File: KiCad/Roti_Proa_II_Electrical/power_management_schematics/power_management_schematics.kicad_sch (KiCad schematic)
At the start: 0 parts

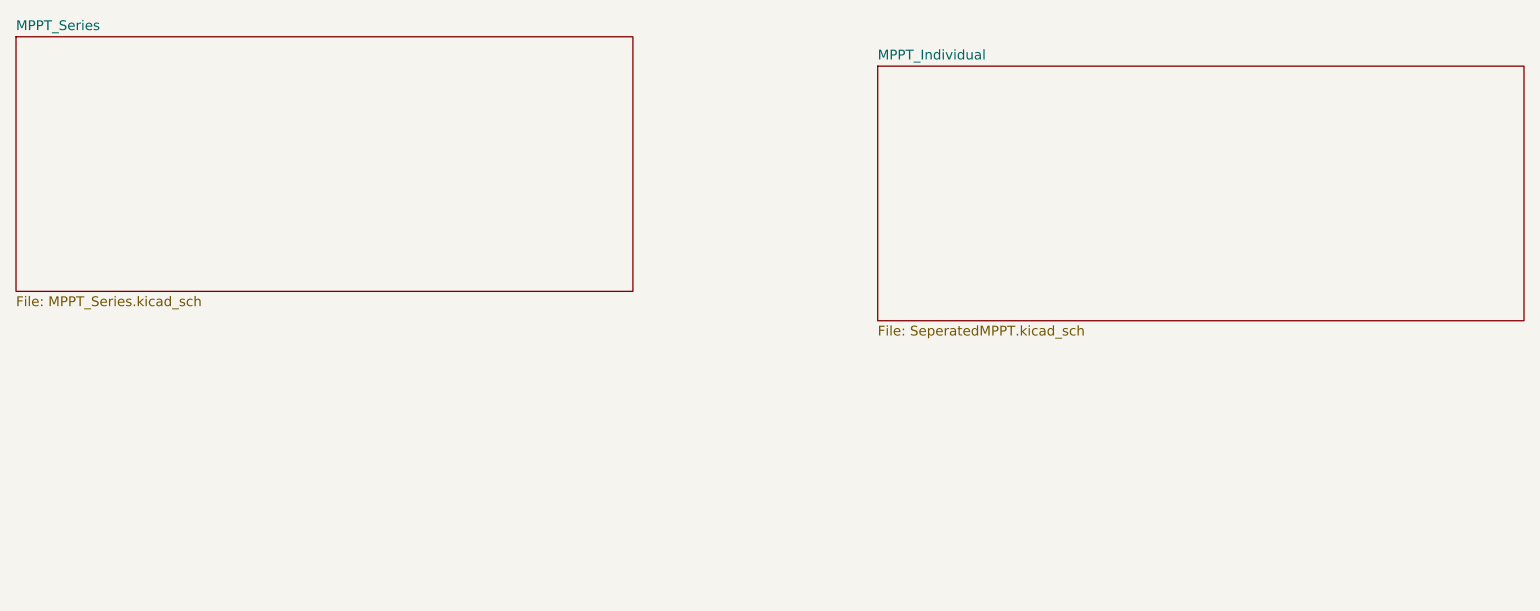
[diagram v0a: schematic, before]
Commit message: Complete MPPT+HE reading
Reading works for arduino and esp8266
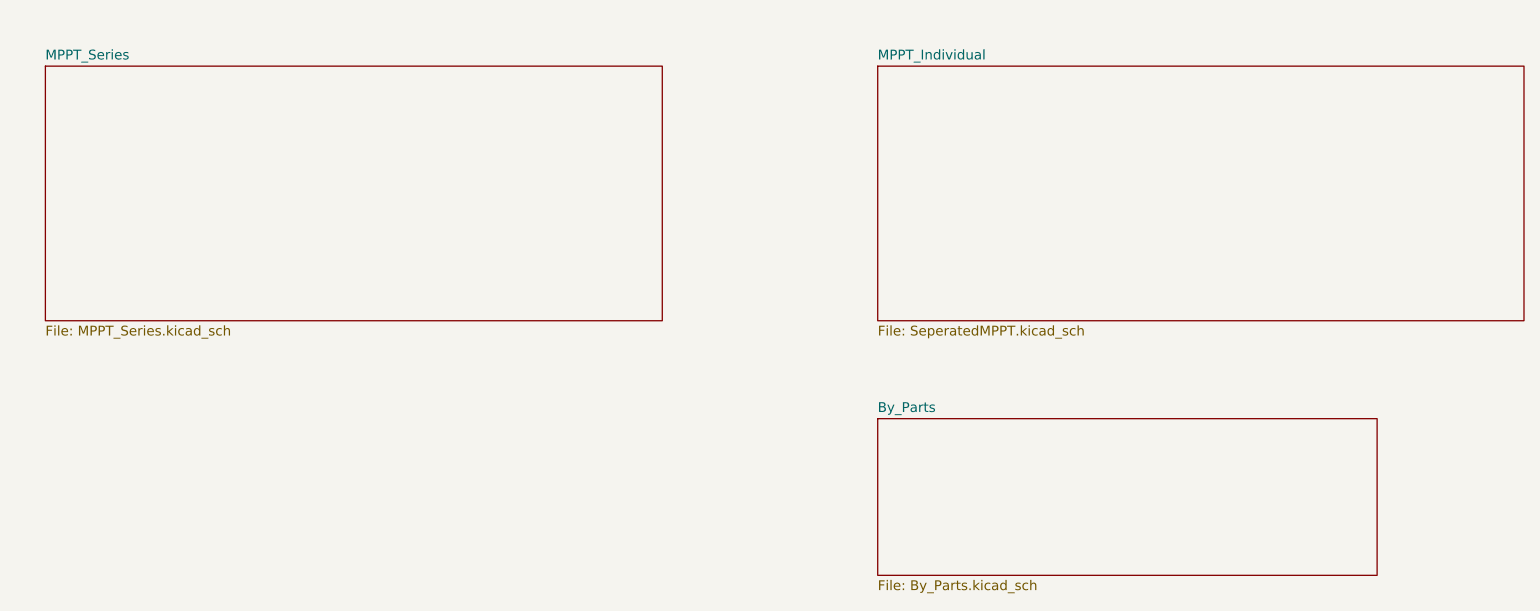
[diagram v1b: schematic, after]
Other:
- added sheet By_Parts (By_Parts.kicad_sch)
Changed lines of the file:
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@@
 	)
 	(sheet
-		(at 40.64 50.8)
+		(at 44.45 54.61)
 		(size 80.01 33.02)
-		(exclude_from_sim no)
-		(in_bom yes)
-		(on_board yes)
-		(dnp no)
+		(exclude_from_sim yes)
+		(in_bom no)
+		(on_board no)
+		(dnp yes)
 		(fields_autoplaced yes)
 		(stroke
@@
 		)
 		(property "Sheetname" "MPPT_Series"
-			(at 40.64 50.0884 0)
+			(at 44.45 53.8984 0)
 			(effects
 				(font
@@
 		)
 		(property "Sheetfile" "MPPT_Series.kicad_sch"
-			(at 40.64 84.4046 0)
+			(at 44.45 88.2146 0)
 			(effects
 				(font
@@
 				)
 			)
+		)
+	)
+	(sheet
+		(at 152.4 100.33)
+		(size 64.77 20.32)
+		(exclude_from_sim no)
+		(in_bom yes)
+		(on_board yes)
+		(dnp no)
+		(fields_autoplaced yes)
+		(stroke
+			(width 0.1524)
+			(type solid)
+		)
+		(fill
+			(color 0 0 0 0.0000)
+		)
+		(property "Sheetname" "By_Parts"
+			(at 152.4 99.6184 0)
+			(effects
+				(font
+					(size 1.27 1.27)
+				)
+				(justify left bottom)
+			)
+		)
+		(property "Sheetfile" "By_Parts.kicad_sch"
+			(at 152.4 121.2346 0)
+			(effects
+				(font
+					(size 1.27 1.27)
+				)
+				(justify left top)
+			)
+		)
+		(instances
+			(project "power_management_schematics"
+				(path "/2ac0f618-a56d-4d5a-8ee1-064312bcd851"
+					(page "8")
+				)
+			)
